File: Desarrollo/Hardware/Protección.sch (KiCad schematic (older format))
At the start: 51 parts, among them J1 Entradas Analógicas, U1 TPD2E001, U15 TPD2E001, U2 TPD2E001, U3 TPD2E001, U4 TPD2E001, U5 TPD2E001, U6 TPD2E001, U7 TPD2E001, U8 TPD2E001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

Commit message: Actualización final. Serigrafía nueva de jumpers y logos que se habían borrado de PONCHO y OPEN HARDWARE. PLACA TERMINADA.
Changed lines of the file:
@@
 LIBS:xilinx
 LIBS:Zilog
+LIBS:Jumpers_Config
+LIBS:Jumpers_Default
 LIBS:PonchoERG-cache
 EELAYER 25 0
@@
 L +3.3V-RESCUE-PonchoERG #PWR?
 U 1 1 57CB28B5
-P 850 7200
+P 850 7150
 AR Path="/57CB28B5" Ref="#PWR?"  Part="1"
 AR Path="/57BDBDC8/57CB28B5" Ref="#PWR01"  Part="1"
-F 0 "#PWR01" H 850 7050 50  0001 C CNN
-F 1 "+3.3V" H 850 7340 50  0000 C CNN
-F 2 "" H 850 7200 50  0000 C CNN
-F 3 "" H 850 7200 50  0000 C CNN
-	1    850  7200
-	1    0    0    -1
-$EndComp
-$Comp
-L PWR_FLAG #FLG08
+F 0 "#PWR01" H 850 7000 50  0001 C CNN
+F 1 "+3.3V" H 850 7290 50  0000 C CNN
+F 2 "" H 850 7150 50  0000 C CNN
+F 3 "" H 850 7150 50  0000 C CNN
+	1    850  7150
+	1    0    0    -1
+$EndComp
+$Comp
+L PWR_FLAG #FLG02
 U 1 1 57CB771E
-P 2000 7100
-F 0 "#FLG08" H 2000 7195 30  0001 C CNN
-F 1 "PWR_FLAG" H 2000 7280 30  0000 C CNN
-F 2 "" H 2000 7100 60  0000 C CNN
-F 3 "" H 2000 7100 60  0000 C CNN
-	1    2000 7100
+P 2000 7150
+F 0 "#FLG02" H 2000 7245 30  0001 C CNN
+F 1 "PWR_FLAG" H 2000 7330 30  0000 C CNN
+F 2 "" H 2000 7150 60  0000 C CNN
+F 3 "" H 2000 7150 60  0000 C CNN
+	1    2000 7150
 	-1   0    0    1
 $EndComp
@@
 	600  2800 600  600
 Wire Wire Line
-	850  7200 850  7250
+	850  7150 850  7250
 Wire Wire Line
 	850  7250 1200 7250
@@
 $EndComp
 $Comp
-L GNDA #PWR?
+L GNDA #PWR03
 U 1 1 580E2DEF
 P 6400 1900
-F 0 "#PWR?" H 6400 1900 40  0001 C CNN
+F 0 "#PWR03" H 6400 1900 40  0001 C CNN
 F 1 "GNDA" H 6400 1800 40  0000 C CNN
 F 2 "" H 6400 1900 60  0000 C CNN
@@
 $EndComp
 $Comp
-L GNDA #PWR?
+L GNDA #PWR04
 U 1 1 580E4132
 P 6450 3400
-F 0 "#PWR?" H 6450 3400 40  0001 C CNN
+F 0 "#PWR04" H 6450 3400 40  0001 C CNN
 F 1 "GNDA" H 6450 3300 40  0000 C CNN
 F 2 "" H 6450 3400 60  0000 C CNN
@@
 $EndComp
 $Comp
-L GNDA #PWR?
+L GNDA #PWR05
 U 1 1 580E41D6
 P 6450 4900
-F 0 "#PWR?" H 6450 4900 40  0001 C CNN
+F 0 "#PWR05" H 6450 4900 40  0001 C CNN
 F 1 "GNDA" H 6450 4800 40  0000 C CNN
 F 2 "" H 6450 4900 60  0000 C CNN
@@
 $EndComp
 $Comp
-L GNDA #PWR?
+L GNDA #PWR06
 U 1 1 580E427A
 P 6450 6400
-F 0 "#PWR?" H 6450 6400 40  0001 C CNN
+F 0 "#PWR06" H 6450 6400 40  0001 C CNN
 F 1 "GNDA" H 6450 6300 40  0000 C CNN
 F 2 "" H 6450 6400 60  0000 C CNN
@@
 $EndComp
 $Comp
-L GNDA #PWR?
+L GNDA #PWR07
 U 1 1 580E431E
 P 9150 4600
-F 0 "#PWR?" H 9150 4600 40  0001 C CNN
+F 0 "#PWR07" H 9150 4600 40  0001 C CNN
 F 1 "GNDA" H 9150 4500 40  0000 C CNN
 F 2 "" H 9150 4600 60  0000 C CNN
@@
 	9150 4550 9150 4600
 $Comp
-L GNDA #PWR?
+L GNDA #PWR08
 U 1 1 580E44F9
 P 1500 7250
-F 0 "#PWR?" H 1500 7250 40  0001 C CNN
+F 0 "#PWR08" H 1500 7250 40  0001 C CNN
 F 1 "GNDA" H 1500 7150 40  0000 C CNN
 F 2 "" H 1500 7250 60  0000 C CNN
@@
 $EndComp
 $Comp
-L GNDA #PWR?
+L GNDA #PWR09
 U 1 1 580E459D
 P 5150 7500
-F 0 "#PWR?" H 5150 7500 40  0001 C CNN
+F 0 "#PWR09" H 5150 7500 40  0001 C CNN
 F 1 "GNDA" H 5150 7400 40  0000 C CNN
 F 2 "" H 5150 7500 60  0000 C CNN
@@
 	1    0    0    -1
 $EndComp
+Wire Wire Line
+	2000 7150 2000 7100
+Connection ~ 2000 7100
 $EndSCHEMATC

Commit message: Actualización de PCB. Cotas de diseño. Generación de BOM. Archivos Gerber disponibles en carpeta "gerbers". Colocación de eje auxiliar de posicionamiento en mounting hole inferior izquierdo. Actualización de esquemático con modificación de comentarios y adición de código de compra DigiKey y hoja de datos en algunos componentes que faltaban. FINALIZADO
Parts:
- R5: Código Digikey (none) -> 311-2.2KARCT-ND
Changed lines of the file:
@@
 F 2 "Resistors_SMD:R_0805" H 5150 2200 50  0001 C CNN
 F 3 "http://www.yageo.com.tw/exep/pages/download/literatures/PYu-R_INT-thick_7.pdf" H 5150 2200 50  0001 C CNN
+F 4 "311-2.2KARCT-ND" V 5150 2200 60  0001 C CNN "Código Digikey"
 	1    5150 2200
 	0    -1   -1   0

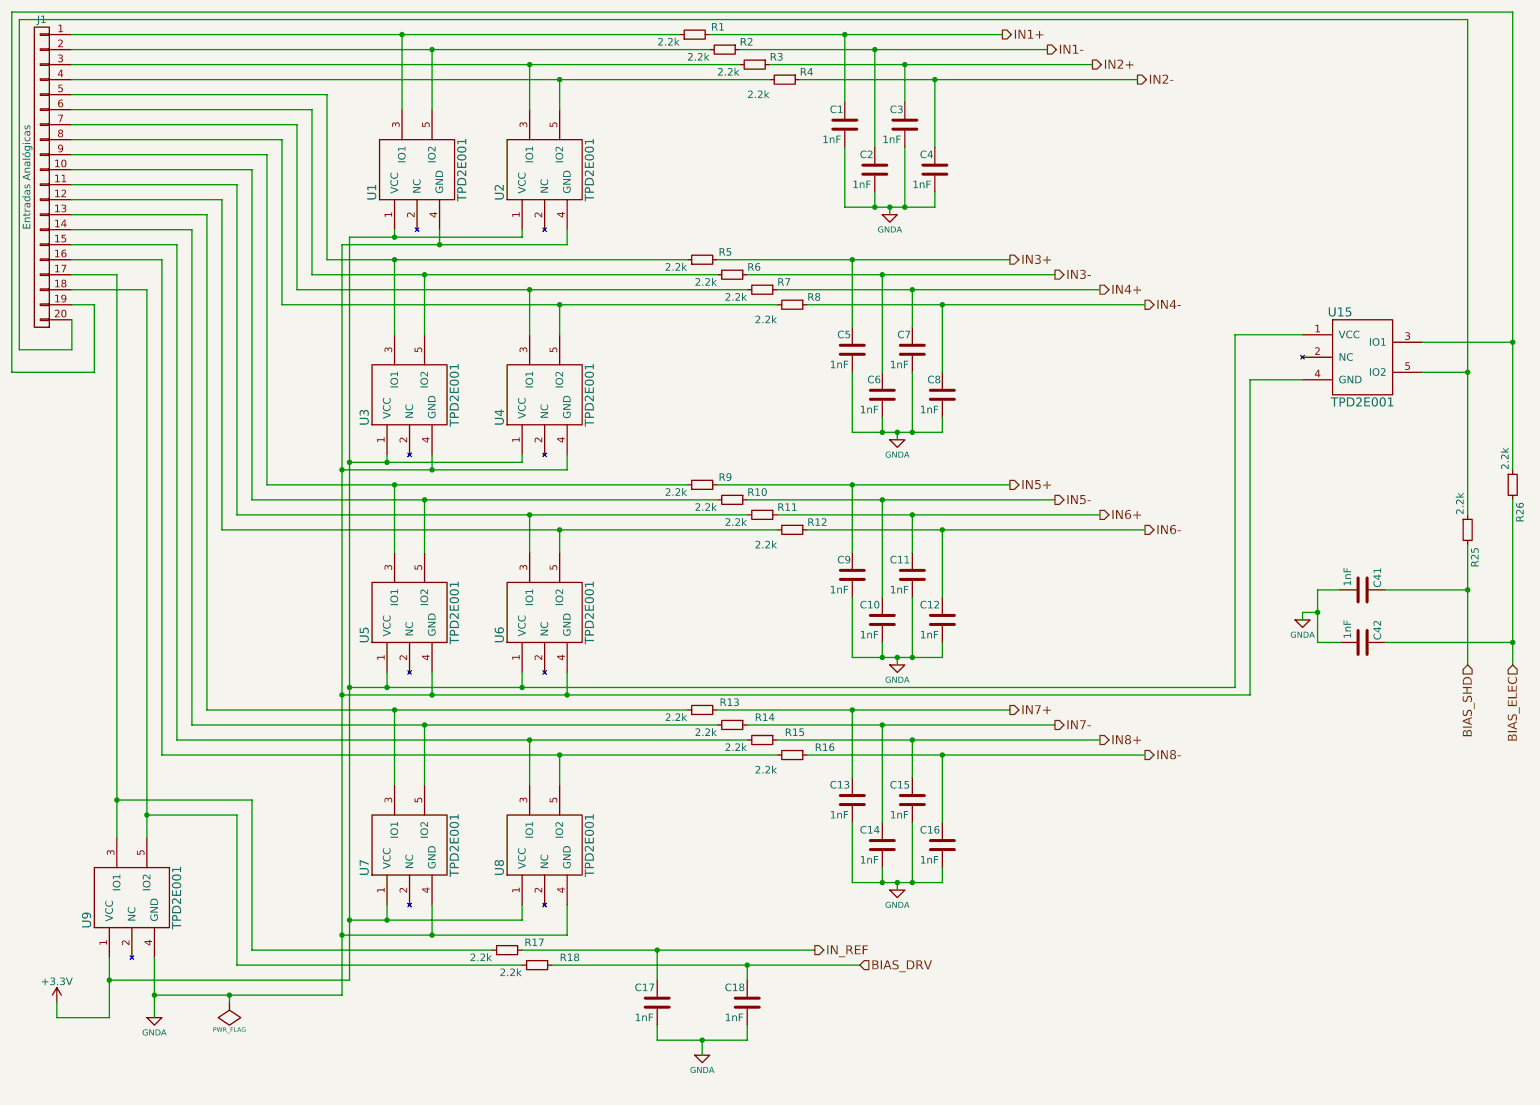
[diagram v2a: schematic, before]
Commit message: - Actualización última versión de Firmware poncho biopotenciales. - Actualización librerías, footprints y otros en Hardware poncho biopotenciales.
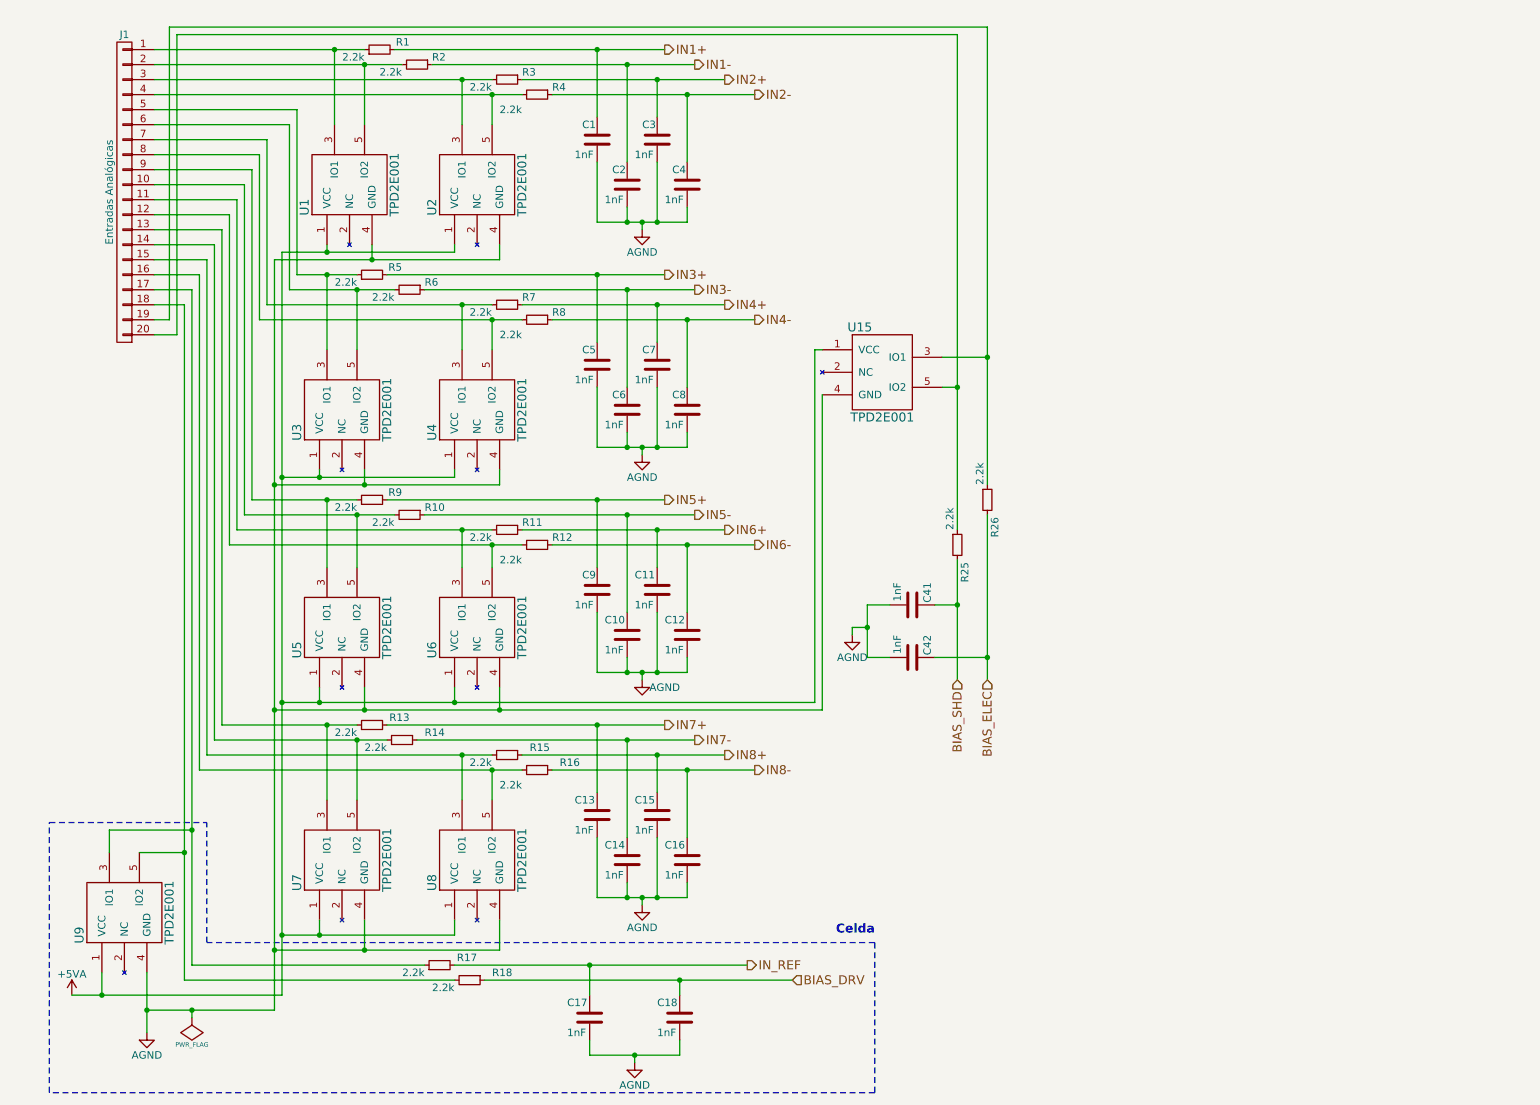
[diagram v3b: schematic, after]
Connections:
- net +3V3 renamed +5VA
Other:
- note added: "Celda"
- moved on the sheet: C1, C10, C11, C12, C13, C14, C15, C16, C17, C18, C2, C3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
